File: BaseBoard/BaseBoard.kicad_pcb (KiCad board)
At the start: 4 copper layers, 50 x 35 mm, 46 parts, among them J1 locked, J2 Serial Port, J3 base connector, Q1 PMN48XP, SW2 boot, SW3 Reset, U1 ESP32-WROOM-E, U3 MCP73831-2ACI-OT, U4 XC6210B332MR

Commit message: Fixes logo reference so it's included in the BaseBoard.
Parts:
- added LOGO1: GameOver_logo, GameOver:logo_fsilk, B.Cu at (149.8, 83.4)
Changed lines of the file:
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@@
     )
+  )
+  (footprint "GameOver:logo_fsilk" (layer "B.Cu")
+    (at 149.8 83.4 180)
+    (property "Sheetfile" "BaseBoard.kicad_sch")
+    (property "Sheetname" "")
+    (property "exclude_from_bom" "")
+    (attr through_hole exclude_from_bom)
+    (fp_text reference "LOGO1" (at 0 0) (layer "B.SilkS") hide
+        (effects (font (size 1.27 1.27) (thickness 0.15)) (justify mirror))
+    )
+    (fp_text value "GameOver_logo" (at 0 0) (layer "B.SilkS") hide
+        (effects (font (size 1.27 1.27) (thickness 0.15)) (justify mirror))
+    )
+    (fp_poly
+      (pts
+        (xy -1.200723 2.388725)
+        (xy -1.041533 2.387945)
+        (xy -0.909803 2.386596)
+        (xy -0.802555 2.384628)
+        (xy -0.716816 2.381995)
+        (xy -0.649611 2.378649)
+        (xy -0.597965 2.374544)
+        (xy -0.558904 2.369633)
+        (xy -0.529451 2.363867)
+        (xy -0.518033 2.360835)
+        (xy -0.450047 2.336304)
+        (xy -0.396715 2.308605)
+        (xy -0.378478 2.293602)
+        (xy -0.368474 2.27151)
+        (xy -0.36026 2.228859)
+        (xy -0.353524 2.16138)
+        (xy -0.347953 2.064803)
+        (xy -0.343238 1.934858)
+        (xy -0.339065 1.767275)
+        (xy -0.338667 1.748346)
+        (xy -0.328083 1.23825)
+        (xy -0.281904 1.312493)
+        (xy -0.24756 1.356772)
+        (xy -0.186966 1.423627)
+        (xy -0.105177 1.508295)
+        (xy -0.007249 1.606012)
+        (xy 0.10176 1.712015)
+        (xy 0.216795 1.82154)
+        (xy 0.3328 1.929824)
+        (xy 0.444718 2.032103)
+        (xy 0.547493 2.123614)
+        (xy 0.636068 2.199594)
+        (xy 0.705388 2.255278)
+        (xy 0.750395 2.285904)
+        (xy 0.752473 2.28697)
+        (xy 0.85725 2.338917)
+        (xy 3.71475 2.338917)
+        (xy 3.836285 2.281959)
+        (xy 3.894983 2.246064)
+        (xy 3.97651 2.184547)
+        (xy 4.075028 2.102913)
+        (xy 4.184698 2.006669)
+        (xy 4.299684 1.901323)
+        (xy 4.414147 1.792379)
+        (xy 4.52225 1.685345)
+        (xy 4.618154 1.585727)
+        (xy 4.696022 1.499032)
+        (xy 4.750017 1.430766)
+        (xy 4.766774 1.40428)
+        (xy 4.788276 1.362652)
+        (xy 4.806603 1.320978)
+        (xy 4.821984 1.275691)
+        (xy 4.834648 1.223223)
+        (xy 4.844824 1.160005)
+        (xy 4.852741 1.08247)
+        (xy 4.858629 0.98705)
+        (xy 4.862715 0.870176)
+        (xy 4.86523 0.728281)
+        (xy 4.866401 0.557795)
+        (xy 4.866459 0.355152)
+        (xy 4.865632 0.116783)
+        (xy 4.864402 -0.116905)
+        (xy 4.85775 -1.281561)
+        (xy 4.788546 -1.42209)
+        (xy 4.762538 -1.470833)
+        (xy 4.731756 -1.518497)
+        (xy 4.691873 -1.569925)
+        (xy 4.63856 -1.629958)
+        (xy 4.567491 -1.70344)
+        (xy 4.474337 -1.795213)
+        (xy 4.354771 -1.910119)
+        (xy 4.338581 -1.92556)
+        (xy 4.203502 -2.052926)
+        (xy 4.093665 -2.153136)
+        (xy 4.005009 -2.229582)
+        (xy 3.933471 -2.285661)
+        (xy 3.874993 -2.324766)
+        (xy 3.836285 -2.345458)
+        (xy 3.71475 -2.402416)
+        (xy 2.31775 -2.406591)
+        (xy 2.0232 -2.40729)
+        (xy 1.768345 -2.407474)
+        (xy 1.550552 -2.407104)
+        (xy 1.367185 -2.406139)
+        (xy 1.21561 -2.404538)
+        (xy 1.093192 -2.402261)
+        (xy 0.997296 -2.399267)
+        (xy 0.925287 -2.395517)
+        (xy 0.874531 -2.390969)
+        (xy 0.842392 -2.385583)
+        (xy 0.836083 -2.383828)
+        (xy 0.767931 -2.359354)
+        (xy 0.708242 -2.333479)
+        (xy 0.699597 -2.329039)
+        (xy 0.662904 -2.302371)
+        (xy 0.601761 -2.250131)
+        (xy 0.521146 -2.177182)
+        (xy 0.426032 -2.088387)
+        (xy 0.321395 -1.98861)
+        (xy 0.212211 -1.882714)
+        (xy 0.103454 -1.775563)
+        (xy 0.000101 -1.672021)
+        (xy -0.092875 -1.57695)
+        (xy -0.170497 -1.495214)
+        (xy -0.227791 -1.431677)
+        (xy -0.259755 -1.391242)
+        (xy -0.328083 -1.285749)
+        (xy -0.339509 -2.180293)
+        (xy -0.450213 -2.253152)
+        (xy -0.528038 -2.297645)
+        (xy -0.609929 -2.334249)
+        (xy -0.656167 -2.349199)
+        (xy -0.695854 -2.354298)
+        (xy -0.770214 -2.358556)
+        (xy -0.880243 -2.361985)
+        (xy -1.026935 -2.364595)
+        (xy -1.211286 -2.366397)
+        (xy -1.434292 -2.367402)
+        (xy -1.696949 -2.367621)
+        (xy -2.000251 -2.367064)
+        (xy -2.233083 -2.366235)
+        (xy -3.71475 -2.360083)
+        (xy -3.835845 -2.303326)
+        (xy -3.89414 -2.267633)
+        (xy -3.975305 -2.206322)
+        (xy -4.073519 -2.124885)
+        (xy -4.182961 -2.028814)
+        (xy -4.297808 -1.923602)
+        (xy -4.412238 -1.814741)
+        (xy -4.52043 -1.707723)
+        (xy -4.616563 -1.608041)
+        (xy -4.694814 -1.521186)
+        (xy -4.749361 -1.452652)
+        (xy -4.767185 -1.424692)
+        (xy -4.788605 -1.383195)
+        (xy -4.806861 -1.341594)
+        (xy -4.822183 -1.296323)
+        (xy -4.834797 -1.243817)
+        (xy -4.844932 -1.180508)
+        (xy -4.852816 -1.102831)
+        (xy -4.858677 -1.007219)
+        (xy -4.862744 -0.890106)
+        (xy -4.865243 -0.747925)
+        (xy -4.866403 -0.577112)
+        (xy -4.866453 -0.374098)
+        (xy -4.865619 -0.135318)
+        (xy -4.864402 0.095739)
+        (xy -4.860288 0.816053)
+        (xy -3.577167 0.816053)
+        (xy -3.577167 -0.792687)
+        (xy -3.434659 -0.936296)
+        (xy -3.292151 -1.079904)
+        (xy -1.280583 -1.068916)
+        (xy -1.274854 -0.640291)
+        (xy -1.269124 -0.211666)
+        (xy -0.381 -0.211666)
+        (xy -0.381 0.306488)
+        (xy 0.529167 0.306488)
+        (xy 0.529167 -0.418632)
+        (xy 0.904367 -0.770232)
+        (xy 1.279568 -1.121833)
+        (xy 3.290354 -1.121833)
+        (xy 3.43376 -0.979526)
+        (xy 3.577167 -0.837218)
+        (xy 3.577167 0.771521)
+        (xy 3.434859 0.914928)
+        (xy 3.292552 1.058334)
+        (xy 1.280142 1.058334)
+        (xy 0.904654 0.682411)
+        (xy 0.529167 0.306488)
+        (xy -0.381 0.306488)
+        (xy -0.381 1.100667)
+        (xy -3.290354 1.100667)
+        (xy -3.433761 0.95836)
+        (xy -3.577167 0.816053)
+        (xy -4.860288 0.816053)
+        (xy -4.85775 1.260395)
+        (xy -4.788884 1.400238)
+        (xy -4.762931 1.448807)
+        (xy -4.732062 1.496472)
+        (xy -4.691962 1.548056)
+        (xy -4.638319 1.608384)
+        (xy -4.566819 1.682278)
+        (xy -4.473148 1.774563)
+        (xy -4.352993 1.890062)
+        (xy -4.33848 1.903909)
+        (xy -4.203118 2.031592)
+        (xy -4.093021 2.132081)
+        (xy -4.004162 2.208743)
+        (xy -3.932514 2.264948)
+        (xy -3.874053 2.304065)
+        (xy -3.835845 2.324494)
+        (xy -3.71475 2.38125)
+        (xy -2.171556 2.387079)
+        (xy -1.872786 2.388111)
+        (xy -1.613374 2.38876)
+        (xy -1.390345 2.388981)
+        (xy -1.200723 2.388725)
+      )
+      (stroke (width 0.01) (type solid)) (fill solid) (layer "B.SilkS"))
   )
   (footprint "Capacitor_SMD:C_0805_2012Metric_Pad1.18x1.45mm_HandSolder" (layer "B.Cu")

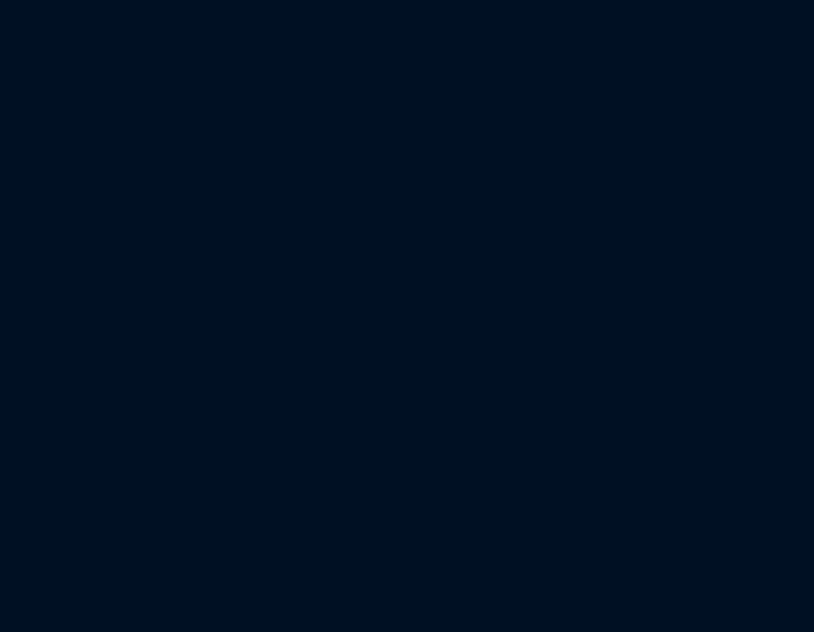
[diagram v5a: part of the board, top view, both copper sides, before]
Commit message: Imports power latch components onto PCB
Also hides the silkscreen references.
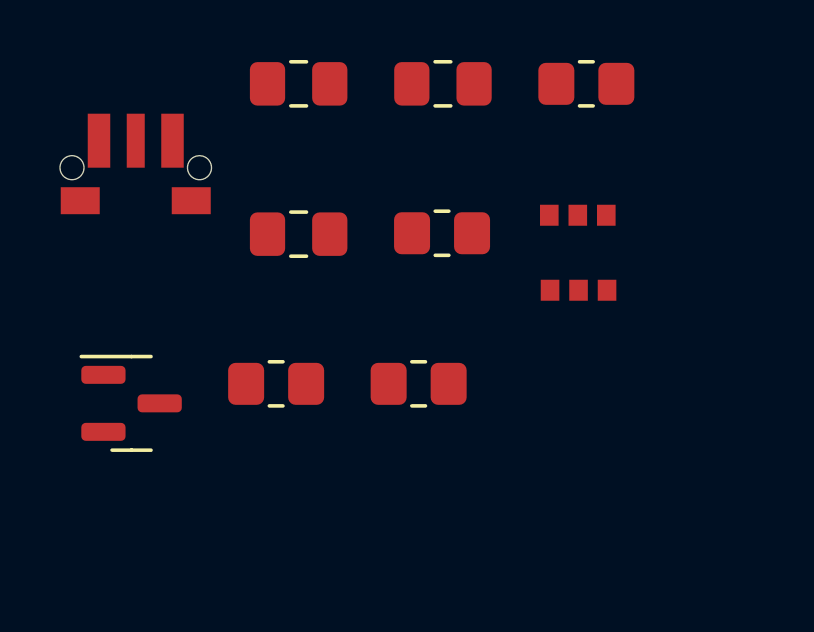
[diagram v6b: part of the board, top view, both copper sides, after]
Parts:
- added C12: 100nF, Capacitor_SMD:C_0805_2012Metric_Pad1.18x1.45mm_HandSolder, F.Cu at (87.8, 72.0)
- added C17: 1µF, Capacitor_SMD:C_0805_2012Metric_Pad1.18x1.45mm_HandSolder, F.Cu at (83.0, 77.0)
- added C8: 1µF, Capacitor_SMD:C_0805_2012Metric_Pad1.18x1.45mm_HandSolder, F.Cu at (83.0, 72.0)
- added D3: BAS20, Package_TO_SOT_SMD:SOT-23, F.Cu at (77.4, 82.7)
- added Q2: SSM6L820R, GameOver:TSOP6F, F.Cu at (92.3, 77.6)
- added R14: 10kΩ, Resistor_SMD:R_0805_2012Metric_Pad1.20x1.40mm_HandSolder, F.Cu at (82.2, 82.0)
- added R15: 100kΩ, Resistor_SMD:R_0805_2012Metric_Pad1.20x1.40mm_HandSolder, F.Cu at (87.8, 77.0)
- added R16: 100kΩ, Resistor_SMD:R_0805_2012Metric_Pad1.20x1.40mm_HandSolder, F.Cu at (87.0, 82.0)
- added R17: 100kΩ, Resistor_SMD:R_0805_2012Metric_Pad1.20x1.40mm_HandSolder, F.Cu at (92.6, 72.0)
- added SW1: Battery switch, GameOver:SW_Tactile_SPST_SOFNG_TS-1814, F.Cu at (77.6, 73.9)
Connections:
- Q1 pad 1: +BATT -> +SWITCHED_BATT
- Q1 pad 2: +BATT -> +SWITCHED_BATT
- Q1 pad 5: +BATT -> +SWITCHED_BATT
- Q1 pad 6: +BATT -> +SWITCHED_BATT

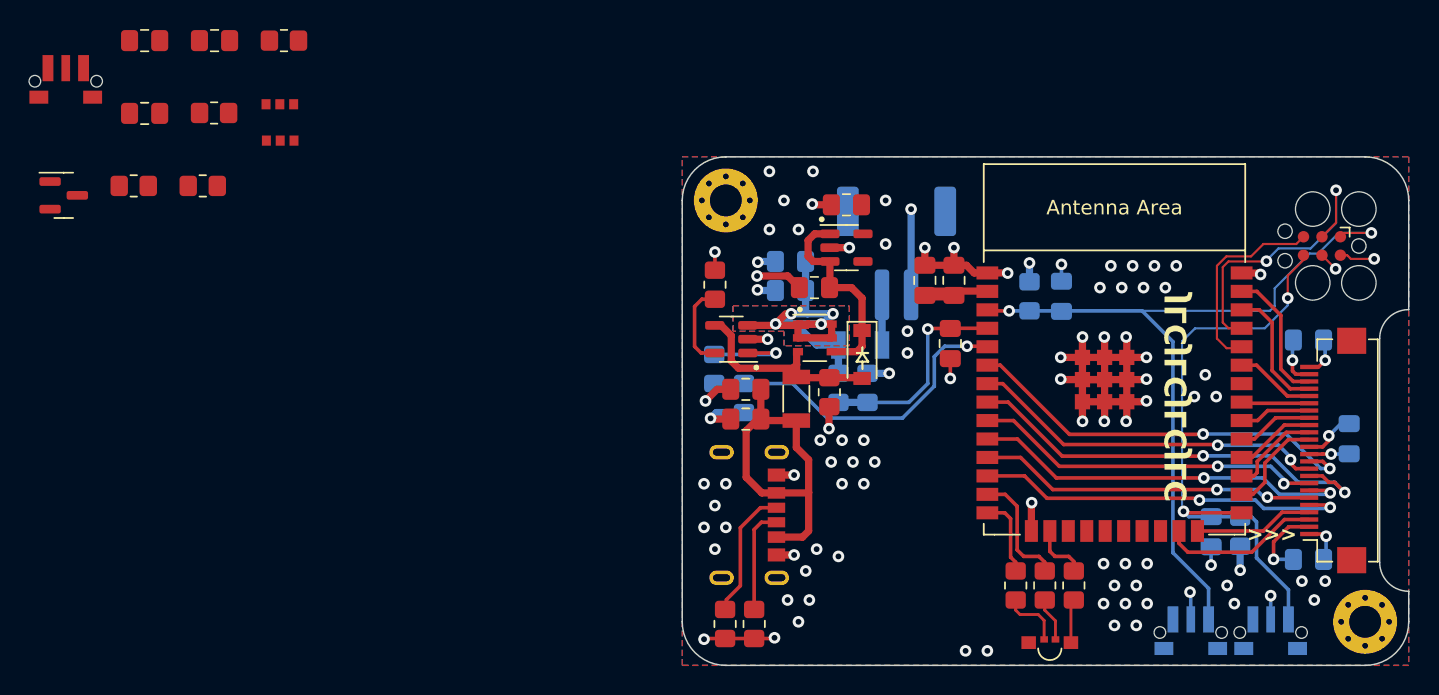
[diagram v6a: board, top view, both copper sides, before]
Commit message: Temporarily removes 3v3 stitching vias
This will make it easier to reroute the power section to include the
switch circuitry.
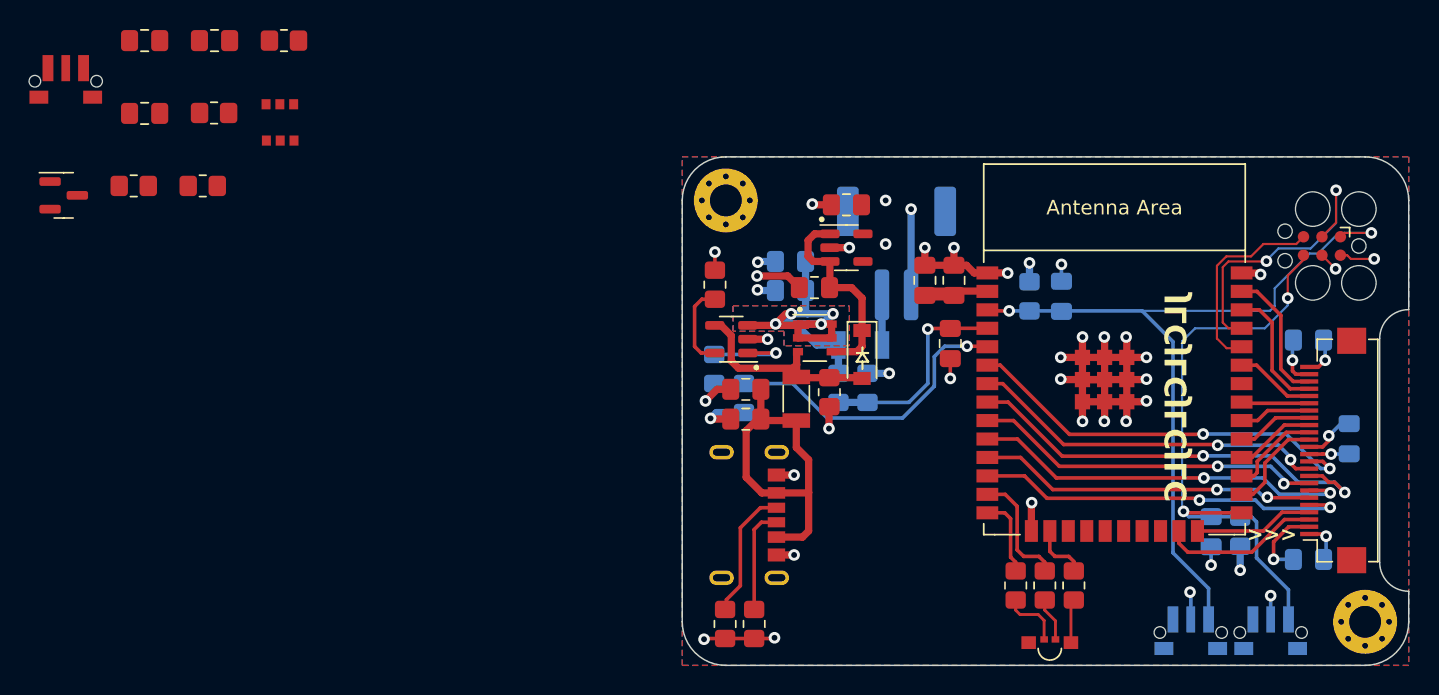
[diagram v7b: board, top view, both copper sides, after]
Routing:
- net +3V3: vias 63 -> 8
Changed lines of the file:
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@@
   (segment (start 163.15 94.96) (end 162.225978 94.96) (width 0.25) (layer "F.Cu") (net 3))
   (segment (start 164.659032 100.454174) (end 164.079848 100.454174) (width 0.25) (layer "F.Cu") (net 3))
-  (via (at 128 112) (size 0.8) (drill 0.4) (layers "F.Cu" "B.Cu") (free) (net 3))
-  (via (at 129.25 107) (size 0.8) (drill 0.4) (layers "F.Cu" "B.Cu") (free) (net 3))
-  (via (at 123 105.5) (size 0.8) (drill 0.4) (layers "F.Cu" "B.Cu") (free) (net 3))
-  (via (at 135.5 92) (size 0.8) (drill 0.4) (layers "F.Cu" "B.Cu") (free) (net 3))
-  (via (at 132.5 99.5) (size 0.8) (drill 0.4) (layers "F.Cu" "B.Cu") (free) (net 3))
-  (via (at 150.5 110.75) (size 0.8) (drill 0.4) (layers "F.Cu" "B.Cu") (free) (net 3))
-  (via (at 131 99.5) (size 0.8) (drill 0.4) (layers "F.Cu" "B.Cu") (free) (net 3))
-  (via (at 156 95) (size 0.8) (drill 0.4) (layers "F.Cu" "B.Cu") (free) (net 3))
-  (via (at 127.25 110.5) (size 0.8) (drill 0.4) (layers "F.Cu" "B.Cu") (free) (net 3))
-  (via (at 141 114) (size 0.8) (drill 0.4) (layers "F.Cu" "B.Cu") (free) (net 3))
-  (via (at 126 81) (size 0.8) (drill 0.4) (layers "F.Cu" "B.Cu") (free) (net 3))
-  (via (at 129.5 99.5) (size 0.8) (drill 0.4) (layers "F.Cu" "B.Cu") (free) (net 3))
-  (via (at 162.65 109.2) (size 0.8) (drill 0.4) (layers "F.Cu" "B.Cu") (free) (net 3))
-  (via (at 149.75 112.25) (size 0.8) (drill 0.4) (layers "F.Cu" "B.Cu") (free) (net 3))
-  (via (at 151.75 89) (size 0.8) (drill 0.4) (layers "F.Cu" "B.Cu") (free) (net 3))
   (via (at 164.659032 100.454174) (size 0.8) (drill 0.4) (layers "F.Cu" "B.Cu") (net 3))
-  (via (at 131.75 101) (size 0.8) (drill 0.4) (layers "F.Cu" "B.Cu") (free) (net 3))
-  (via (at 149.5 87.5) (size 0.8) (drill 0.4) (layers "F.Cu" "B.Cu") (free) (net 3))
-  (via (at 148.75 89) (size 0.8) (drill 0.4) (layers "F.Cu" "B.Cu") (free) (net 3))
-  (via (at 150.25 89) (size 0.8) (drill 0.4) (layers "F.Cu" "B.Cu") (free) (net 3))
-  (via (at 135.5 93.5) (size 0.8) (drill 0.4) (layers "F.Cu" "B.Cu") (free) (net 3))
-  (via (at 128 85) (size 0.8) (drill 0.4) (layers "F.Cu" "B.Cu") (free) (net 3))
-  (via (at 129 81) (size 0.8) (drill 0.4) (layers "F.Cu" "B.Cu") (free) (net 3))
-  (via (at 127 83) (size 0.8) (drill 0.4) (layers "F.Cu" "B.Cu") (free) (net 3))
-  (via (at 121.5 105.5) (size 0.8) (drill 0.4) (layers "F.Cu" "B.Cu") (free) (net 3))
-  (via (at 122.25 104) (size 0.8) (drill 0.4) (layers "F.Cu" "B.Cu") (free) (net 3))
-  (via (at 151.25 109.5) (size 0.8) (drill 0.4) (layers "F.Cu" "B.Cu") (free) (net 3))
-  (via (at 139.5 114) (size 0.8) (drill 0.4) (layers "F.Cu" "B.Cu") (free) (net 3))
-  (via (at 151 87.5) (size 0.8) (drill 0.4) (layers "F.Cu" "B.Cu") (free) (net 3))
-  (via (at 153.25 89) (size 0.8) (drill 0.4) (layers "F.Cu" "B.Cu") (free) (net 3))
-  (via (at 152 110.75) (size 0.8) (drill 0.4) (layers "F.Cu" "B.Cu") (free) (net 3))
   (via (at 164.313519 106.106257) (size 0.8) (drill 0.4) (layers "F.Cu" "B.Cu") (net 3))
-  (via (at 132.5 102.5) (size 0.8) (drill 0.4) (layers "F.Cu" "B.Cu") (free) (net 3))
-  (via (at 126 85) (size 0.8) (drill 0.4) (layers "F.Cu" "B.Cu") (free) (net 3))
-  (via (at 151.25 112.25) (size 0.8) (drill 0.4) (layers "F.Cu" "B.Cu") (free) (net 3))
-  (via (at 152.5 87.5) (size 0.8) (drill 0.4) (layers "F.Cu" "B.Cu") (free) (net 3))
-  (via (at 149 110.75) (size 0.8) (drill 0.4) (layers "F.Cu" "B.Cu") (free) (net 3))
-  (via (at 128.5 108.5) (size 0.8) (drill 0.4) (layers "F.Cu" "B.Cu") (free) (net 3))
-  (via (at 149 108) (size 0.8) (drill 0.4) (layers "F.Cu" "B.Cu") (free) (net 3))
-  (via (at 154 87.5) (size 0.8) (drill 0.4) (layers "F.Cu" "B.Cu") (free) (net 3))
-  (via (at 133.25 101) (size 0.8) (drill 0.4) (layers "F.Cu" "B.Cu") (free) (net 3))
   (via (at 134 83) (size 0.8) (drill 0.4) (layers "F.Cu" "B.Cu") (free) (net 3))
-  (via (at 157.5 109.5) (size 0.8) (drill 0.4) (layers "F.Cu" "B.Cu") (free) (net 3))
-  (via (at 163.5 110.5) (size 0.8) (drill 0.4) (layers "F.Cu" "B.Cu") (free) (net 3))
-  (via (at 164.25 109.2) (size 0.8) (drill 0.4) (layers "F.Cu" "B.Cu") (free) (net 3))
-  (via (at 131 102.5) (size 0.8) (drill 0.4) (layers "F.Cu" "B.Cu") (free) (net 3))
   (via (at 167.625 87.024251) (size 0.8) (drill 0.4) (layers "F.Cu" "B.Cu") (net 3))
-  (via (at 122.25 107) (size 0.8) (drill 0.4) (layers "F.Cu" "B.Cu") (free) (net 3))
-  (via (at 158 110.75) (size 0.8) (drill 0.4) (layers "F.Cu" "B.Cu") (free) (net 3))
-  (via (at 150.5 108) (size 0.8) (drill 0.4) (layers "F.Cu" "B.Cu") (free) (net 3))
-  (via (at 130.25 101) (size 0.8) (drill 0.4) (layers "F.Cu" "B.Cu") (free) (net 3))
   (via (at 143.9 87.3) (size 0.8) (drill 0.4) (layers "F.Cu" "B.Cu") (net 3))
-  (via (at 121.5 102.5) (size 0.8) (drill 0.4) (layers "F.Cu" "B.Cu") (free) (net 3))
   (via (at 162 94) (size 0.8) (drill 0.4) (layers "F.Cu" "B.Cu") (net 3))
-  (via (at 123 102.5) (size 0.8) (drill 0.4) (layers "F.Cu" "B.Cu") (free) (net 3))
   (via (at 134 86) (size 0.8) (drill 0.4) (layers "F.Cu" "B.Cu") (free) (net 3))
-  (via (at 155.25 96.5) (size 0.8) (drill 0.4) (layers "F.Cu" "B.Cu") (free) (net 3))
-  (via (at 128.75 110.5) (size 0.8) (drill 0.4) (layers "F.Cu" "B.Cu") (free) (net 3))
-  (via (at 156.75 96.5) (size 0.8) (drill 0.4) (layers "F.Cu" "B.Cu") (free) (net 3))
   (via (at 158.4 108.45) (size 0.8) (drill 0.4) (layers "F.Cu" "B.Cu") (net 3))
-  (via (at 149.75 109.5) (size 0.8) (drill 0.4) (layers "F.Cu" "B.Cu") (free) (net 3))
-  (via (at 130.75 107.5) (size 0.8) (drill 0.4) (layers "F.Cu" "B.Cu") (free) (net 3))
-  (via (at 152 108) (size 0.8) (drill 0.4) (layers "F.Cu" "B.Cu") (free) (net 3))
   (segment (start 164.659032 100.454174) (end 165.883326 100.454174) (width 0.25) (layer "B.Cu") (net 3))
   (segment (start 162 94) (end 162 92.6725) (width 0.25) (layer "B.Cu") (net 3))
